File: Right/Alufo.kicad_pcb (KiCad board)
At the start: 2 copper layers, 139.7 x 88.9 mm, 67 parts, among them J2 USB_C_Receptacle_USB2.0_16P_2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, J4 USB_C_Receptacle_USB2.0_16P_2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, K11 PG1350, K12 PG1350, K13 PG1350, K14 PG1350, K15 PG1350, K16 PG1350, K21 PG1350, K22 PG1350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

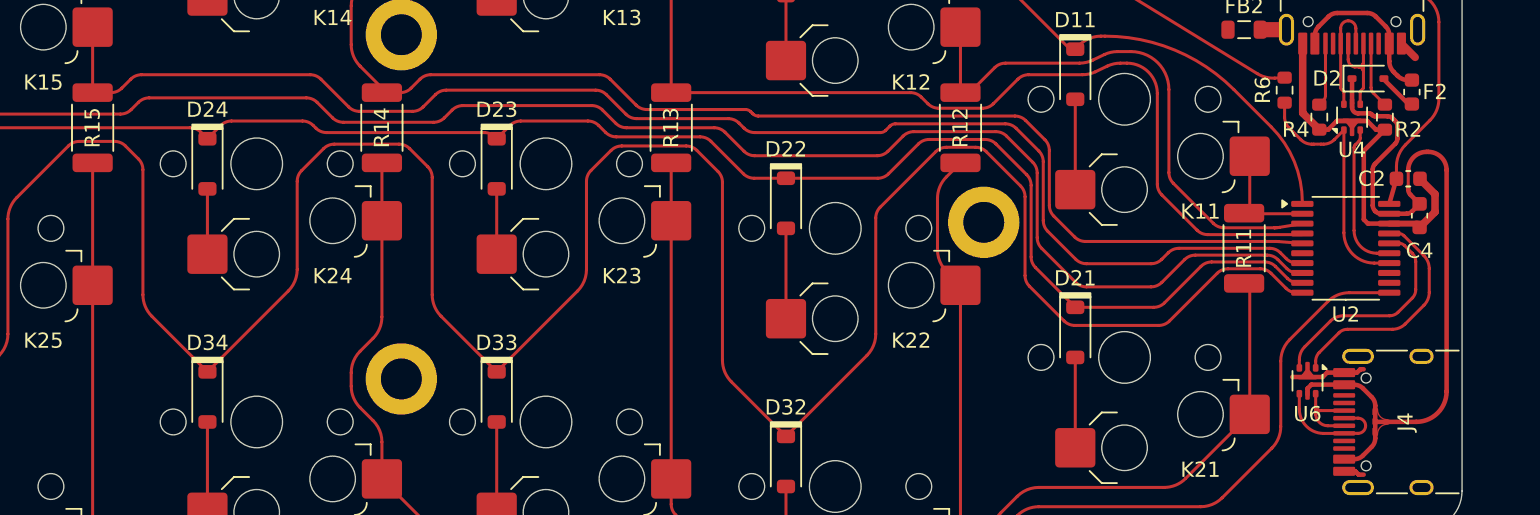
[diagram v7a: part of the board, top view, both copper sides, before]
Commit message: Power routing tweaks
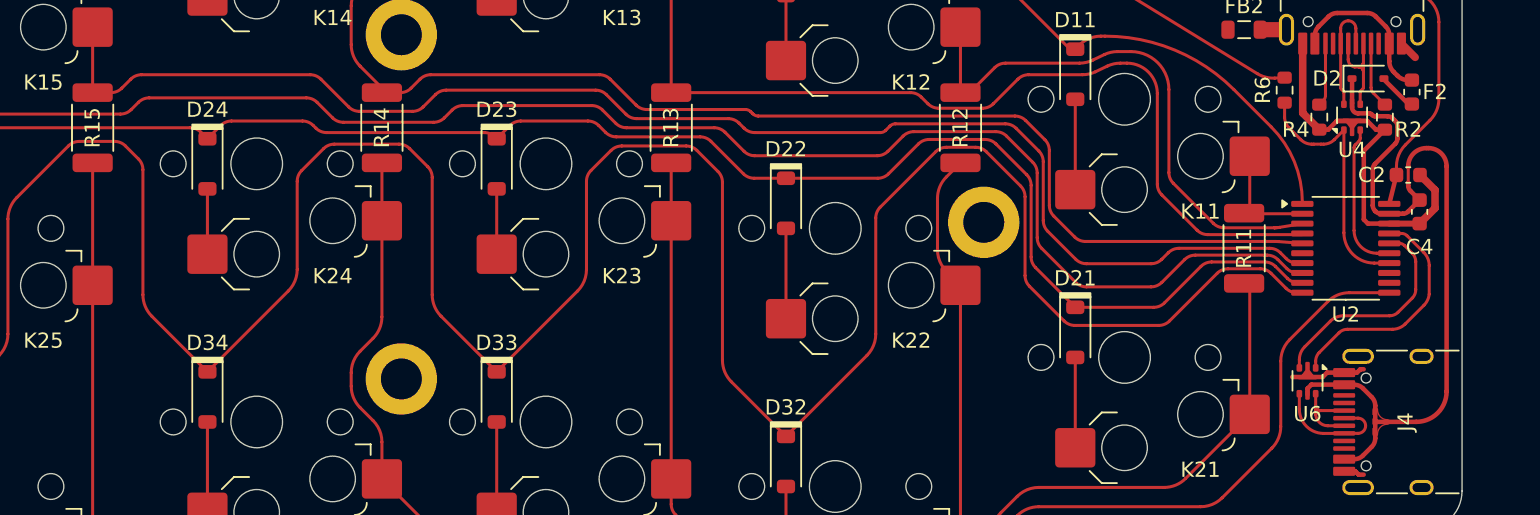
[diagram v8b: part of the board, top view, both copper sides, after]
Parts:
- moved C4 0.25 mm to (219.5, 59.8)
- moved C2 0.25 mm to (218.7, 57.4)
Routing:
- net Col5: track 93.6 -> 92.4 mm
- net RX: track 14.9 -> 15.6 mm
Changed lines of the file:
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@@
 	(footprint "Capacitor_SMD:C_0603_1608Metric"
 		(layer "F.Cu")
-		(at 218.706 57.652296)
+		(at 218.706 57.404)
 		(descr "Capacitor SMD 0603 (1608 Metric), square (rectangular) end terminal, IPC_7351 nominal, (Body size source: IPC-SM-782 page 76, https://www.pcb-3d.com/wordpress/wp-content/uploads/ipc-sm-782a_amendment_1_and_2.pdf), generated with kicad-footprint-generator")
 		(tags "capacitor")
@@
 	(footprint "Capacitor_SMD:C_0603_1608Metric"
 		(layer "F.Cu")
-		(at 219.456 60.08 -90)
+		(at 219.456 59.83 -90)
 		(descr "Capacitor SMD 0603 (1608 Metric), square (rectangular) end terminal, IPC_7351 nominal, (Body size source: IPC-SM-782 page 76, https://www.pcb-3d.com/wordpress/wp-content/uploads/ipc-sm-782a_amendment_1_and_2.pdf), generated with kicad-footprint-generator")
 		(tags "capacitor")
@@
 	)
 	(segment
-		(start 219.456 60.855)
-		(end 220.472 59.839)
-		(width 0.5)
-		(layer "F.Cu")
-		(net 10)
-	)
-	(segment
 		(start 214.747656 53.844)
 		(end 213.993 53.844)
@@
 	)
 	(segment
-		(start 220.472 58.668296)
-		(end 219.456 57.652296)
-		(width 0.5)
+		(start 217.458 60.605)
+		(end 219.329 60.605)
+		(width 0.4)
 		(layer "F.Cu")
 		(net 10)
 	)
 	(segment
-		(start 217.458 60.605)
-		(end 219.329 60.605)
-		(width 0.4)
+		(start 216.008 53.844)
+		(end 216.583 54.419)
+		(width 0.3)
 		(layer "F.Cu")
 		(net 10)
 	)
 	(segment
-		(start 220.472 59.839)
-		(end 220.472 58.668296)
+		(start 220.472 59.589)
+		(end 220.472 58.395)
 		(width 0.5)
 		(layer "F.Cu")
@@
 	)
 	(segment
-		(start 216.008 53.844)
-		(end 216.583 54.419)
-		(width 0.3)
+		(start 219.456 60.605)
+		(end 220.472 59.589)
+		(width 0.5)
 		(layer "F.Cu")
 		(net 10)
@@
 	)
 	(segment
+		(start 220.472 58.395)
+		(end 219.481 57.404)
+		(width 0.5)
+		(layer "F.Cu")
+		(net 10)
+	)
+	(segment
 		(start 215.333316 70.416684)
 		(end 215.519 70.231)
@@
 	)
 	(segment
-		(start 184.059593 36.116677)
-		(end 177.859593 36.116677)
-		(width 0.2)
+		(start 217.458 59.305)
+		(end 217.931 57.404)
+		(width 0.3)
 		(layer "F.Cu")
 		(net 19)
 	)
 	(segment
-		(start 218.726 45.333344)
-		(end 210.147839 45.333344)
+		(start 184.059593 36.116677)
+		(end 177.859593 36.116677)
 		(width 0.2)
 		(layer "F.Cu")
@@
 	)
 	(segment
-		(start 217.931 57.652296)
-		(end 217.931 56.836427)
+		(start 218.726 45.333344)
+		(end 210.147839 45.333344)
 		(width 0.2)
 		(layer "F.Cu")
@@
 	)
 	(segment
-		(start 217.458 59.305)
-		(end 217.931 57.652296)
-		(width 0.3)
+		(start 217.931 56.836427)
+		(end 217.931 57.404)
+		(width 0.2)
 		(layer "F.Cu")
 		(net 19)
@@
 	)
 	(segment
-		(start 218.952447 59.808553)
-		(end 219.456 59.305)
+		(start 214.488 71.216684)
+		(end 215.156629 71.216684)
 		(width 0.3)
 		(layer "F.Cu")
@@
 	)
 	(segment
-		(start 214.488 71.216684)
-		(end 215.156629 71.216684)
+		(start 212.074 71.882)
+		(end 212.074 71.464344)
 		(width 0.3)
 		(layer "F.Cu")
@@
 	)
 	(segment
-		(start 212.074 71.882)
-		(end 212.074 71.464344)
+		(start 218.705999 56.831704)
+		(end 218.705999 56.890296)
 		(width 0.3)
 		(layer "F.Cu")
@@
 	)
 	(segment
-		(start 219.234 73.66)
-		(end 216.535 73.66)
-		(width 0.3)
-		(layer "F.Cu")
-		(net 21)
-	)
-	(segment
-		(start 218.705999 57.138592)
-		(end 218.705999 58.166)
+		(start 218.705999 56.890296)
+		(end 218.705999 57.917704)
 		(width 0.2)
 		(layer "F.Cu")
@@
 	)
 	(segment
-		(start 218.705999 57.138592)
-		(end 218.705999 57.08)
-		(width 0.3)
-		(layer "F.Cu")
-		(net 21)
-	)
-	(segment
-		(start 221.234 57.08)
-		(end 221.234 71.66)
-		(width 0.3)
-		(layer "F.Cu")
-		(net 21)
-	)
-	(segment
-		(start 219.456 59.305)
-		(end 218.852445 58.701445)
+		(start 216.506907 53.535422)
+		(end 217.337673 53.535422)
 		(width 0.3)
 		(layer "F.Cu")
@@
 	)
 	(segment
-		(start 216.506907 53.535422)
-		(end 217.337673 53.535422)
+		(start 217.458 59.955)
+		(end 218.348893 59.955)
 		(width 0.3)
 		(layer "F.Cu")
@@
 	)
 	(segment
-		(start 216.291229 53.402587)
-		(end 216.365486 53.476844)
+		(start 218.702447 59.808553)
+		(end 219.456 59.055)
 		(width 0.3)
 		(layer "F.Cu")
@@
 	)
 	(segment
-		(start 218.705999 58.347892)
-		(end 218.705999 58.166)
+		(start 216.291229 53.402587)
+		(end 216.365486 53.476844)
 		(width 0.3)
 		(layer "F.Cu")
@@
 	)
 	(segment
-		(start 219.905999 55.88)
-		(end 220.034 55.88)
+		(start 221.234 56.831704)
+		(end 221.234 71.66)
 		(width 0.3)
 		(layer "F.Cu")
@@
 	)
 	(segment
-		(start 217.458 59.955)
-		(end 218.598893 59.955)
+		(start 219.905999 55.631704)
+		(end 220.034 55.631704)
 		(width 0.3)
 		(layer "F.Cu")
@@
 	)
 	(segment
+		(start 219.234 73.66)
+		(end 216.535 73.66)
+		(width 0.3)
+		(layer "F.Cu")
+		(net 21)
+	)
+	(segment
 		(start 216.516947 59.757547)
 		(end 216.567954 59.808554)
@@
 	)
 	(segment
-		(start 215.008 52.669)
-		(end 215.008 52.944008)
+		(start 218.705999 58.097892)
+		(end 218.705999 57.917704)
 		(width 0.3)
 		(layer "F.Cu")
 		(net 21)
 	)
-	(arc
-		(start 218.852445 58.701445)
-		(mid 218.744059 58.539233)
-		(end 218.705999 58.347892)
+	(segment
+		(start 215.008 52.669)
+		(end 215.008 52.944008)
 		(width 0.3)
 		(layer "F.Cu")
 		(net 21)
 	)
-	(arc
-		(start 219.234 73.66)
-		(mid 220.648214 73.074214)
-		(end 221.234 71.66)
+	(segment
+		(start 219.456 59.055)
+		(end 218.852445 58.451445)
 		(width 0.3)
 		(layer "F.Cu")
@@
 	)
 	(arc
-		(start 220.034 55.88)
-		(mid 220.882528 56.231472)
-		(end 221.234 57.08)
+		(start 220.034 55.631704)
+		(mid 220.882528 55.983176)
+		(end 221.234 56.831704)
 		(width 0.3)
 		(layer "F.Cu")
@@
 	)
 	(arc
-		(start 218.705999 57.08)
-		(mid 219.057471 56.231472)
-		(end 219.905999 55.88)
+		(start 218.705999 56.831704)
+		(mid 219.057471 55.983176)
+		(end 219.905999 55.631704)
 		(width 0.3)
 		(layer "F.Cu")
@@
 	)
 	(arc
+		(start 218.348893 59.955)
+		(mid 218.540235 59.91694)
+		(end 218.702447 59.808553)
+		(width 0.3)
+		(layer "F.Cu")
+		(net 21)
+	)
+	(arc
+		(start 218.705999 58.097892)
+		(mid 218.744059 58.289233)
+		(end 218.852445 58.451445)
+		(width 0.3)
+		(layer "F.Cu")
+		(net 21)
+	)
+	(arc
+		(start 221.234 71.66)
+		(mid 220.648214 73.074214)
+		(end 219.234 73.66)
+		(width 0.3)
+		(layer "F.Cu")
+		(net 21)
+	)
+	(arc
 		(start 217.995 54.991376)
 		(mid 217.95694 55.182718)
@@
 	)
 	(arc
-		(start 218.952447 59.808553)
-		(mid 218.790235 59.91694)
-		(end 218.598893 59.955)
-		(width 0.3)
-		(layer "F.Cu")
-		(net 21)
-	)
-	(arc
 		(start 216.516947 59.757547)
 		(mid 216.40856 59.595335)
@@
 	)
 	(segment
-		(start 133.280607 51.979179)
-		(end 132.07 51.979179)
-		(width 0.2)
-		(layer "F.Cu")
-		(net 63)
-	)
-	(segment
 		(start 201.769786 63.246)
 		(end 197.518214 63.246)
@@
 	)
 	(segment
-		(start 220.091 63.565256)
-		(end 220.091 65.134793)
+		(start 218.627447 61.401447)
+		(end 219.73683 62.51083)
+		(width 0.2)
+		(layer "F.Cu")
+		(net 67)
+	)
+	(segment
+		(start 220.088302 63.359358)
+		(end 220.088302 65.252717)
 		(width 0.2)
 		(layer "F.Cu")
@@
 	)
 	(segment
-		(start 218.424247 61.401447)
-		(end 219.739528 62.716728)
+		(start 219.739528 65.983321)
+		(end 218.510321 67.212528)
 		(width 0.2)
 		(layer "F.Cu")
@@
 	)
 	(segment
-		(start 219.739528 65.983321)
-		(end 218.510321 67.212528)
+		(start 217.458 61.255)
+		(end 218.273893 61.255)
 		(width 0.2)
 		(layer "F.Cu")
@@
 	)
 	(arc
-		(start 214.141685 67.798315)
-		(mid 214.401224 67.624896)
-		(end 214.707371 67.564)
+		(start 220.088302 63.359358)
+		(mid 219.996957 62.900138)
+		(end 219.73683 62.51083)
 		(width 0.2)
 		(layer "F.Cu")
@@
 	)
 	(arc
-		(start 219.739528 65.983321)
-		(mid 219.999655 65.594013)
-		(end 220.091 65.134793)
+		(start 214.707371 67.564)
+		(mid 214.401224 67.624896)
+		(end 214.141685 67.798315)
 		(width 0.2)
 		(layer "F.Cu")
@@
 	)
 	(arc
-		(start 212.845814 69.094186)
-		(mid 212.672396 69.353725)
-		(end 212.6115 69.659871)
+		(start 220.088302 65.252717)
+		(mid 219.975785 65.647859)
+		(end 219.739528 65.983321)
 		(width 0.2)
 		(layer "F.Cu")
@@
 	)
 	(arc
-		(start 218.070693 61.255)
-		(mid 218.262035 61.29306)
-		(end 218.424247 61.401447)
+		(start 218.627447 61.401447)
+		(mid 218.465235 61.29306)
+		(end 218.273893 61.255)
 		(width 0.2)
 		(layer "F.Cu")
@@
 	)
 	(arc
-		(start 219.739528 62.716728)
-		(mid 219.999655 63.106036)
-		(end 220.091 63.565256)
+		(start 212.845814 69.094186)
+		(mid 212.672396 69.353725)
+		(end 212.6115 69.659871)
 		(width 0.2)
 		(layer "F.Cu")
